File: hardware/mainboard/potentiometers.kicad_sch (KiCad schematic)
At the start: 6 parts, among them SW2 BUTTON

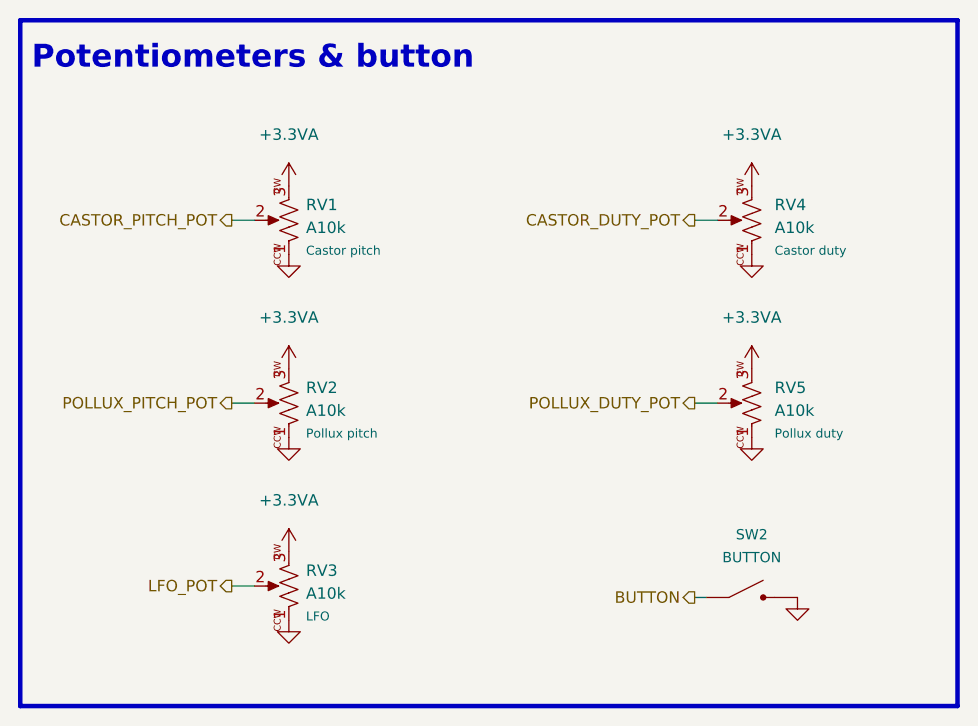
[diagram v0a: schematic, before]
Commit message: hardware: update some labels, fix some fields, re-do fancytext
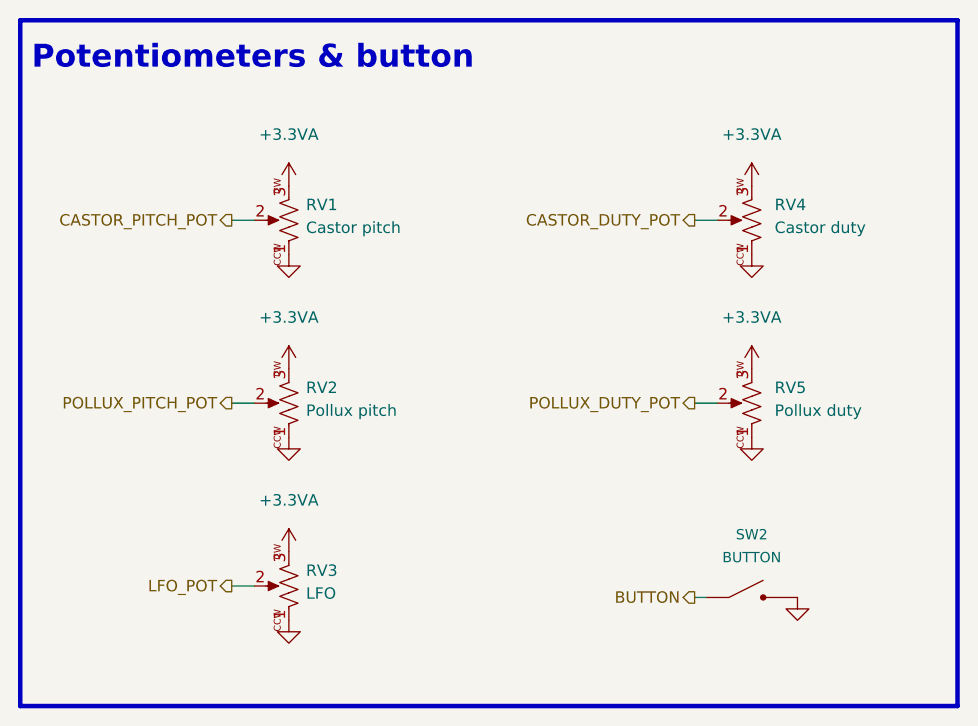
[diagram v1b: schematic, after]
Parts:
- RV1: value A10k -> Castor pitch; Function Castor pitch -> (none); Rating (none) -> A10k
- RV2: value A10k -> Pollux pitch; Function Pollux pitch -> (none); Rating (none) -> A10k
- RV3: value A10k -> LFO; Function LFO -> (none); Rating (none) -> A10k
- RV4: value A10k -> Castor duty; Function Castor duty -> (none); Rating (none) -> A10k
- RV5: value A10k -> Pollux duty; Function Pollux duty -> (none); Rating (none) -> A10k
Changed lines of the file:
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@@
       (effects (font (size 1.27 1.27)) (justify left))
     )
-    (property "Value" "A10k" (id 1) (at 101.6 61.1504 90)
+    (property "Value" "Pollux duty" (id 1) (at 101.6 61.1504 90)
       (effects (font (size 1.27 1.27)) (justify left))
     )
@@
       (effects (font (size 1.27 1.27)) hide)
     )
-    (property "Function" "Pollux duty" (id 7) (at 101.6 63.6905 90)
-      (effects (font (size 1 1)) (justify left))
+    (property "Rating" "A10k" (id 8) (at 99.06 60.325 0)
+      (effects (font (size 1.27 1.27)) hide)
     )
     (pin "1")
@@
       (effects (font (size 0.508 0.508)) (justify left) hide)
     )
-    (property "Datasheet" "" (id 3) (at 99.06 81.915 0)
+    (property "Datasheet" "https://sten-eswitch-13110800-production.s3.amazonaws.com/system/asset/product_line/data_sheet/144/TL1105.pdf" (id 3) (at 99.06 81.915 0)
       (effects (font (size 1.524 1.524)) hide)
     )
@@
       (effects (font (size 1.27 1.27)) (justify left))
     )
-    (property "Value" "A10k" (id 1) (at 49.53 61.1504 90)
+    (property "Value" "Pollux pitch" (id 1) (at 49.53 61.1504 90)
       (effects (font (size 1.27 1.27)) (justify left))
     )
@@
       (effects (font (size 1.27 1.27)) hide)
     )
-    (property "Function" "Pollux pitch" (id 7) (at 49.53 63.6905 90)
-      (effects (font (size 1 1)) (justify left))
+    (property "Rating" "A10k" (id 8) (at 47.625 60.325 0)
+      (effects (font (size 1.27 1.27)) hide)
     )
     (pin "1")
@@
       (effects (font (size 1.27 1.27)) (justify left))
     )
-    (property "Value" "A10k" (id 1) (at 49.53 40.8304 90)
+    (property "Value" "Castor pitch" (id 1) (at 49.53 40.8304 90)
       (effects (font (size 1.27 1.27)) (justify left))
     )
@@
       (effects (font (size 1.27 1.27)) hide)
     )
-    (property "Function" "Castor pitch" (id 7) (at 49.53 43.3705 90)
-      (effects (font (size 1 1)) (justify left))
+    (property "Rating" "A10k" (id 8) (at 47.625 40.005 0)
+      (effects (font (size 1.27 1.27)) hide)
     )
     (pin "1")
@@
       (effects (font (size 1.27 1.27)) (justify left))
     )
-    (property "Value" "A10k" (id 1) (at 101.6 40.8304 90)
+    (property "Value" "Castor duty" (id 1) (at 101.6 40.8304 90)
       (effects (font (size 1.27 1.27)) (justify left))
     )
@@
       (effects (font (size 1.27 1.27)) hide)
     )
-    (property "Function" "Castor duty" (id 7) (at 101.6 43.3705 90)
-      (effects (font (size 1 1)) (justify left))
+    (property "Rating" "A10k" (id 8) (at 99.06 40.005 0)
+      (effects (font (size 1.27 1.27)) hide)
     )
     (pin "1")
@@
       (effects (font (size 1.27 1.27)) (justify left))
     )
-    (property "Value" "A10k" (id 1) (at 49.53 81.4704 90)
+    (property "Value" "LFO" (id 1) (at 49.53 81.4704 90)
       (effects (font (size 1.27 1.27)) (justify left))
     )
@@
       (effects (font (size 1.27 1.27)) hide)
     )
-    (property "Function" "LFO" (id 7) (at 49.53 84.0105 90)
-      (effects (font (size 1 1)) (justify left))
-    )
-    (pin "1")
+    (property "Rating" "A10k" (id 8) (at 47.625 80.645 0)
+      (effects (font (size 1.27 1.27)) hide)
+    )
+    (pin "1")
